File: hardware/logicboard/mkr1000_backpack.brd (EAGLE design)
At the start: 25 x 61.5 mm, 12 parts, among them J3 3.3V, J4 DNP, J5 DNP

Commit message: SparkFun Triple Axis Accelerometer Breakout - H3LIS331DL Ready.
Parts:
- removed RN3: 680, resistor-net:RN-5
- removed RN4: 6.8k, resistor-net:RN-5
- added DUMMY, I2C: (no value), SparkFun-Connectors:1X04
- added R1, R2: 680, resistor:0204/5
- added R3, R4: 6.8k, resistor:0204/5
- moved C1 13.6 mm to (20.5, 52.0)
- moved J3 10.0 mm to (12.5, 21.0)
- moved IPADDRESS 9.00 mm to (12.5, 37.0)
- moved RN2 7.28 mm to (19.5, 37.0), turned to 270 degrees
- moved RN1 7.07 mm to (5.50, 37.0), turned to 270 degrees
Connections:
- net GND: now also I2C.1
- net N$1: now also R1.1; no longer RN3.2
- net N$2: now also R2.1; no longer RN3.3
- net SCL: now also I2C.4, R4.1; no longer RN4.2
- net SDA: now also I2C.3, R3.1; no longer RN4.3
- net VCC: now also I2C.2, R1.2, R2.2, R3.2, R4.2; no longer RN3.1, RN4.1
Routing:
- net GND: track 49.2 -> 110.6 mm, vias 1 -> 2
- net A0: track 23.0 -> 55.4 mm
- net SCL: track 18.5 -> 44.5 mm
- net VCC: track 71.7 -> 93.7 mm
- net A4: track 29.2 -> 47.3 mm, vias 0 -> 1
- net A3: track 44.2 -> 30.3 mm, vias 0 -> 1
- net N$1: track 21.0 -> 8.90 mm
- net D2: track 20.5 -> 32.6 mm, vias 0 -> 1
- net A5: track 43.8 -> 55.7 mm, vias 0 -> 1
- net A2: track 33.8 -> 22.4 mm
- net D3: track 21.7 -> 32.9 mm, vias 1 -> 3
- net A1: track 34.8 -> 23.8 mm
- net SDA: track 21.3 -> 31.4 mm
- net D0: track 18.7 -> 27.3 mm, vias 0 -> 2
- net D1: track 12.3 -> 20.6 mm
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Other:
- board text added: "MKR1000BP 2.0.0 Pineapple"
- board text removed: "MKR1000BP 1.1.0 Pineapple"

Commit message: MMA8452Q
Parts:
- removed DUMMY, I2C: (no value), SparkFun-Connectors:1X04
- added MMA8452Q: (no value), SparkFun-Connectors:1X06_NO_SILK
- moved C1 23.4 mm to (12.5, 30.0)
- moved R3 13.4 mm to (5.00, 22.0), flipped to the bottom
- moved R1 6.71 mm to (11.0, 13.0), flipped to the bottom
- moved R2 6.71 mm to (14.0, 13.0), flipped to the bottom
- moved R4 6.00 mm to (20.0, 22.0), flipped to the bottom
- moved J3 1.00 mm to (12.5, 20.0)
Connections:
- new net D6: J5.1, MMA8452Q.5
- net D7: now also MMA8452Q.4
- net GND: now also MMA8452Q.6; no longer I2C.1
- net SCL: now also MMA8452Q.3; no longer I2C.4
- net SDA: now also MMA8452Q.2; no longer I2C.3
- net VCC: now also MMA8452Q.1; no longer I2C.2
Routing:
- net D3: track 32.9 -> 92.0 mm, vias 3 -> 2
- net GND: track 110.6 -> 56.8 mm, vias 2 -> 0
- net A6: track 55.4 -> 105.6 mm, vias 1 -> 6
- net D2: track 32.6 -> 73.2 mm, vias 1 -> 0
- net A5: track 55.7 -> 94.7 mm, vias 1 -> 4
- net D6: track 0.00 -> 27.2 mm, vias 0 -> 3
- net A1: track 23.8 -> 49.0 mm, vias 0 -> 2
- net SCL: track 44.5 -> 20.3 mm
- net D7: track 17.5 -> 38.7 mm
- net N$2: track 12.9 -> 4.75 mm
- net A3: track 30.3 -> 22.9 mm, vias 1 -> 0
- net VCC: track 93.7 -> 100.2 mm, vias 0 -> 2
- net A2: track 22.4 -> 27.0 mm
- net A4: track 47.3 -> 43.6 mm, vias 1 -> 3
- net N$1: track 8.90 -> 5.52 mm
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
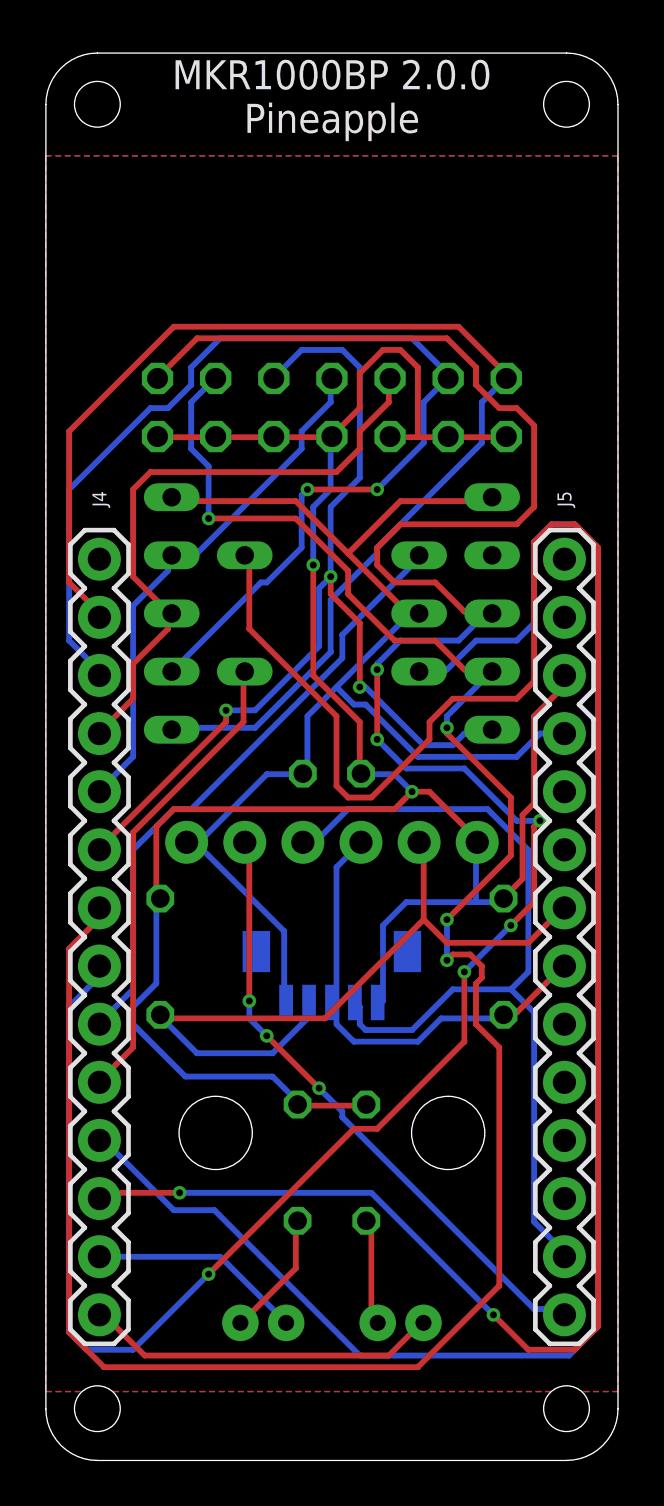
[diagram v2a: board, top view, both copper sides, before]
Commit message: Fixed position of pinheader.
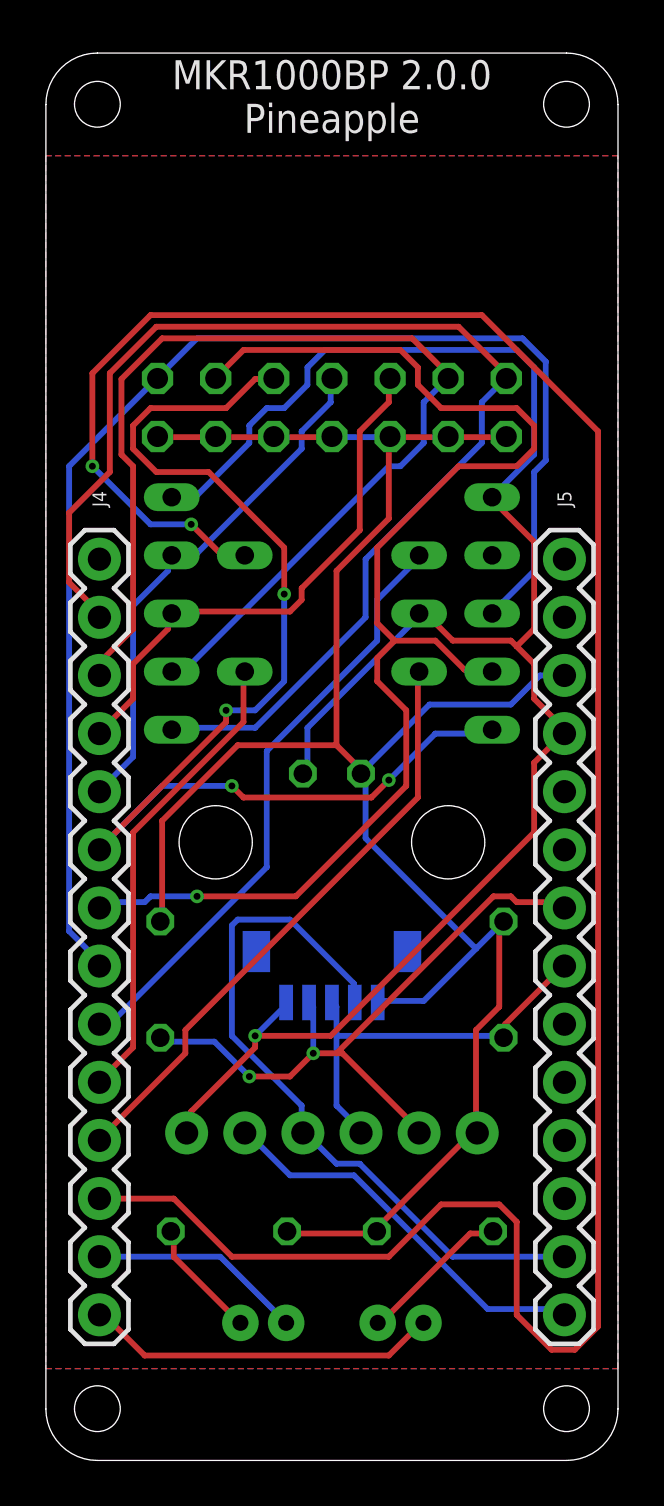
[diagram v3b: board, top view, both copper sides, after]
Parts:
- moved MMA8452Q 12.7 mm to (18.9, 14.3)
- moved R1 4.24 mm to (8.00, 10.0), turned to 180 degrees
- moved R2 4.24 mm to (17.0, 10.0), turned to 0 degrees
- moved R3 1.00 mm to (5.00, 21.0)
- moved R4 1.00 mm to (20.0, 21.0)
- renumbered J1 to LED1, J2 to LED2, J3 to I2C
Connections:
- net N$1 renamed LED1A
- net N$2 renamed LED2A
- net N$3 renamed LED1K
- net N$4 renamed LED2K
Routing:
- net A6: track 105.6 -> 57.9 mm, vias 6 -> 0
- net D2: track 73.2 -> 26.2 mm
- net A5: track 94.7 -> 57.9 mm, vias 4 -> 1
- net GND: track 56.8 -> 80.6 mm, vias 0 -> 1
- net D3: track 92.0 -> 105.9 mm
- net D6: track 27.2 -> 17.3 mm, vias 3 -> 0
- net A4: track 43.6 -> 53.5 mm, vias 3 -> 4
- net VCC: track 100.2 -> 92.5 mm, vias 2 -> 0
- net D7: track 38.7 -> 31.4 mm
- net SDA: track 32.6 -> 29.4 mm, vias 0 -> 2
- net A2: track 27.0 -> 23.8 mm
- net SCL: track 20.3 -> 17.8 mm
- net LED2A: track 4.75 -> 6.66 mm
- net A1: track 49.0 -> 48.0 mm, vias 2 -> 0
